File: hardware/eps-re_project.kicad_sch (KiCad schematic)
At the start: 20 parts, among them J1 2053380004, J13 53398-0671, J14 53398-0471, J2 2053380004, J21 205338-0002, J22 205338-0002, J25 205338-0002, J26 205338-0002, J27 205338-0002, J28 205338-0002, J29 205338-0002, J3 53398-0671, J4 2053380004, J5 53398-0471, J6 53398-0471, J7 53398-0471

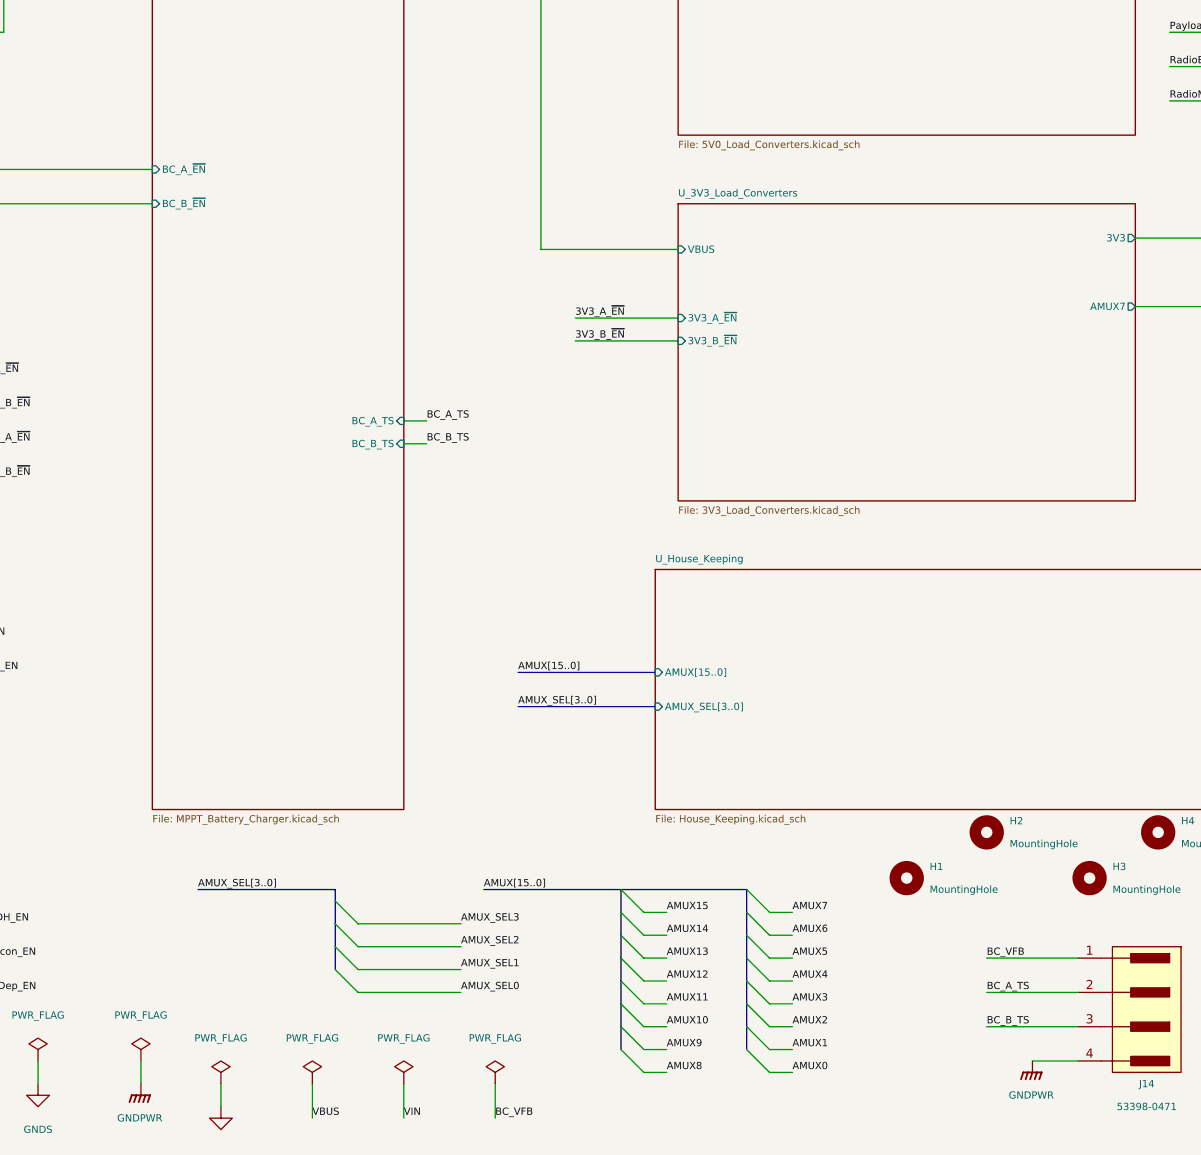
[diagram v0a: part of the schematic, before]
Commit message: hardware: Updating the position of some connectors and components.
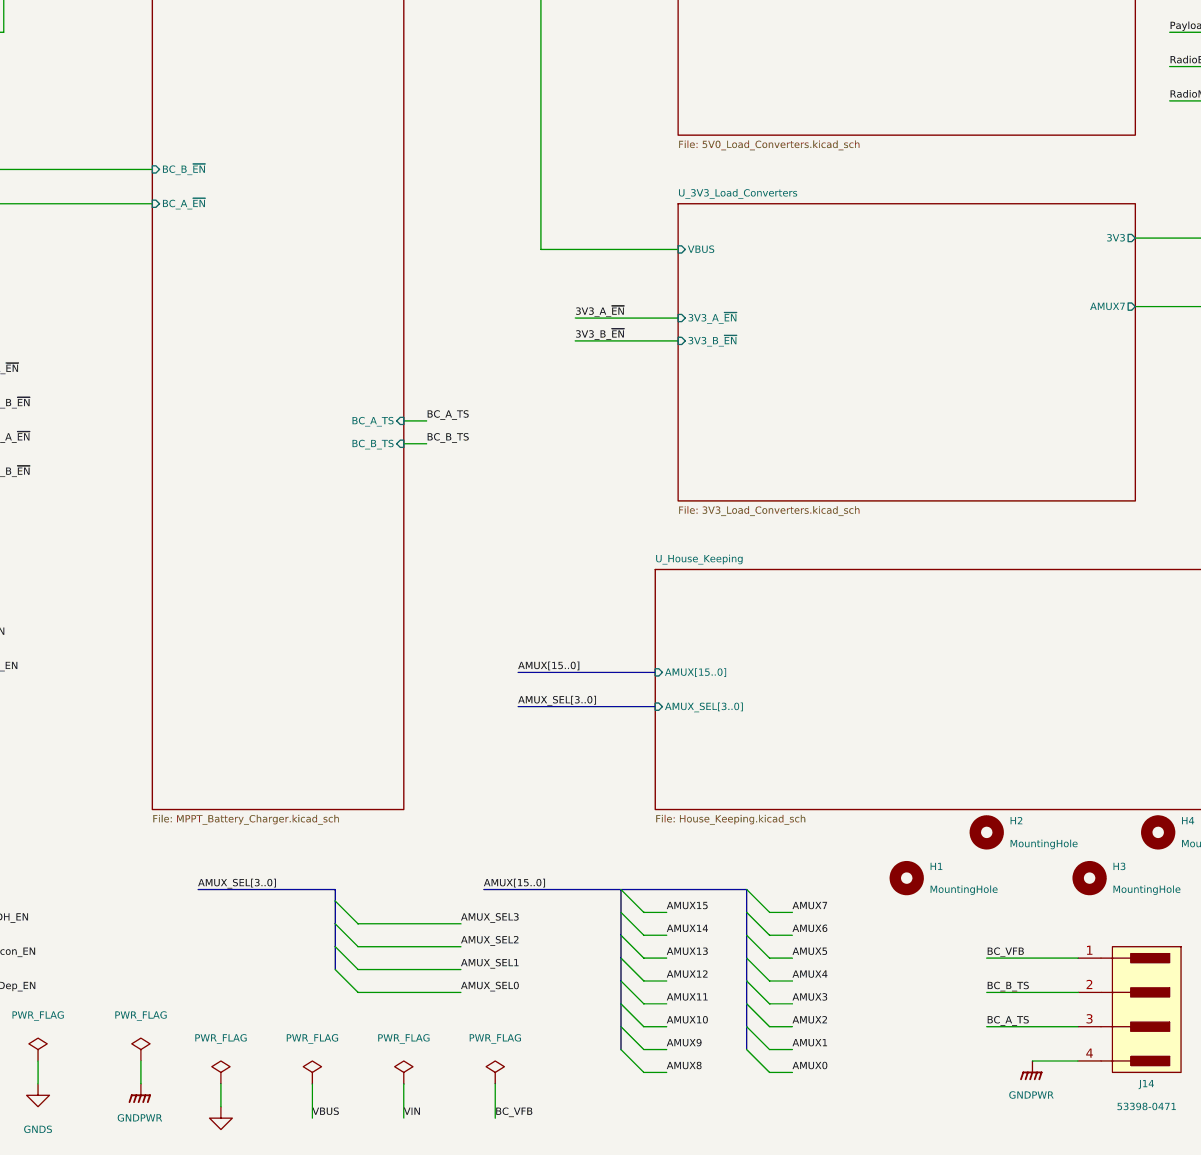
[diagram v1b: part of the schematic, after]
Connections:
- net BC_A_TS: now also J14.3; no longer J14.2
- net BC_B_TS: now also J14.2; no longer J14.3
- net U_MPPT_Batery_Charger/BC_A_~{EN}: now also J5.2; no longer J5.1
- net U_MPPT_Batery_Charger/BC_B_~{EN}: now also J5.1; no longer J5.2
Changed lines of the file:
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@@
     (stroke (width 0) (type default))
   )
-  (wire (pts (xy 29.21 90.17) (xy 57.15 90.17))
-    (stroke (width 0) (type default))
-  )
   (wire (pts (xy 250.19 63.5) (xy 250.19 74.93))
     (stroke (width 0.5) (type default))
@@
     (stroke (width 1) (type default))
   )
-  (wire (pts (xy 29.21 93.98) (xy 57.15 93.98))
+  (wire (pts (xy 29.21 90.17) (xy 57.15 90.17))
     (stroke (width 0) (type default))
   )
@@
     (stroke (width 0.5) (type default))
   )
+  (wire (pts (xy 29.21 93.98) (xy 57.15 93.98))
+    (stroke (width 0) (type default))
+  )
   (wire (pts (xy 170.18 82.55) (xy 186.69 82.55))
     (stroke (width 0) (type default))
@@
     (effects (font (size 0.8 0.8)) (justify left bottom))
   )
-  (label "BC_B_TS" (at 149.86 185.42 0) (fields_autoplaced)
+  (label "BC_A_TS" (at 149.86 185.42 0) (fields_autoplaced)
     (effects (font (size 0.8 0.8)) (justify left bottom))
   )
@@
     (effects (font (size 0.8 0.8)) (justify left bottom))
   )
-  (label "BC_A_TS" (at 149.86 181.61 0) (fields_autoplaced)
+  (label "BC_B_TS" (at 149.86 181.61 0) (fields_autoplaced)
     (effects (font (size 0.8 0.8)) (justify left bottom))
   )
@@
       (effects (font (size 0.8 0.8)) (justify left))
     )
-    (pin "BC_A_~{EN}" input (at 57.15 90.17 180)
+    (pin "BC_A_~{EN}" input (at 57.15 93.98 180)
       (effects (font (size 0.8 0.8)) (justify left))
     )
-    (pin "BC_B_~{EN}" input (at 57.15 93.98 180)
+    (pin "BC_B_~{EN}" input (at 57.15 90.17 180)
       (effects (font (size 0.8 0.8)) (justify left))
     )

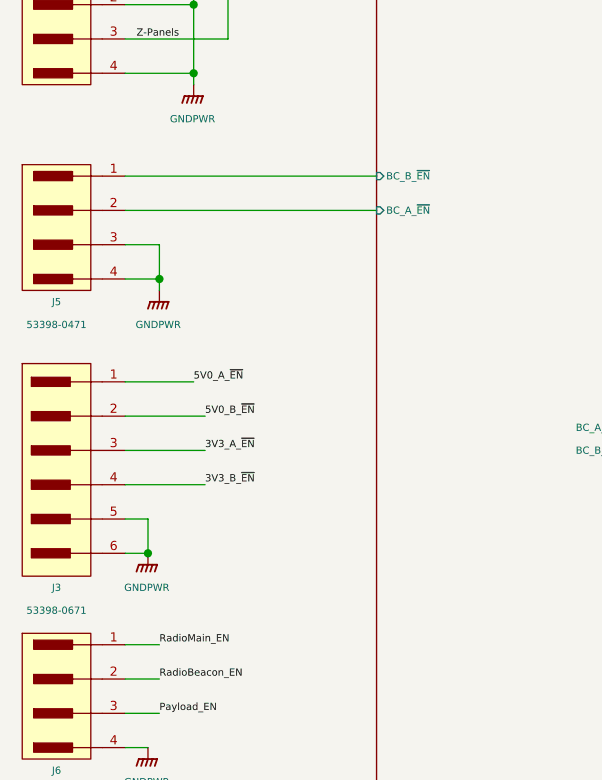
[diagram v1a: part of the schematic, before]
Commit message: hardware: Updating the connectors and connections of the analog signals.
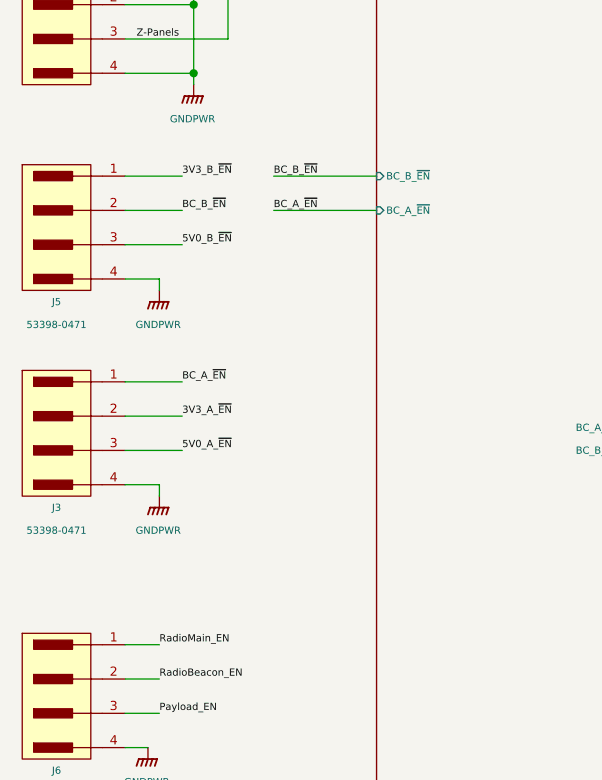
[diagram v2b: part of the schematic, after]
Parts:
- removed J3: 53398-0671, footprints:533980671, symbol 533980671:53398-0671
- added J3: 53398-0471, footprints:533980471, symbol 533980471:533980471_1
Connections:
- net U_MPPT_Batery_Charger/BC_B_~{EN} is gone; now on net 3V3_B_~{EN}: J5.1
- net 3V3_A_~{EN}: now also J3.2
- net 5V0_A_~{EN}: now also J3.3
- net 5V0_B_~{EN}: now also J5.3
- net GNDPWR: now also J3.4; no longer J5.3
- net U_MPPT_Batery_Charger/BC_A_~{EN} renamed BC_B_~{EN}
- new net BC_A_~{EN}: J3.1

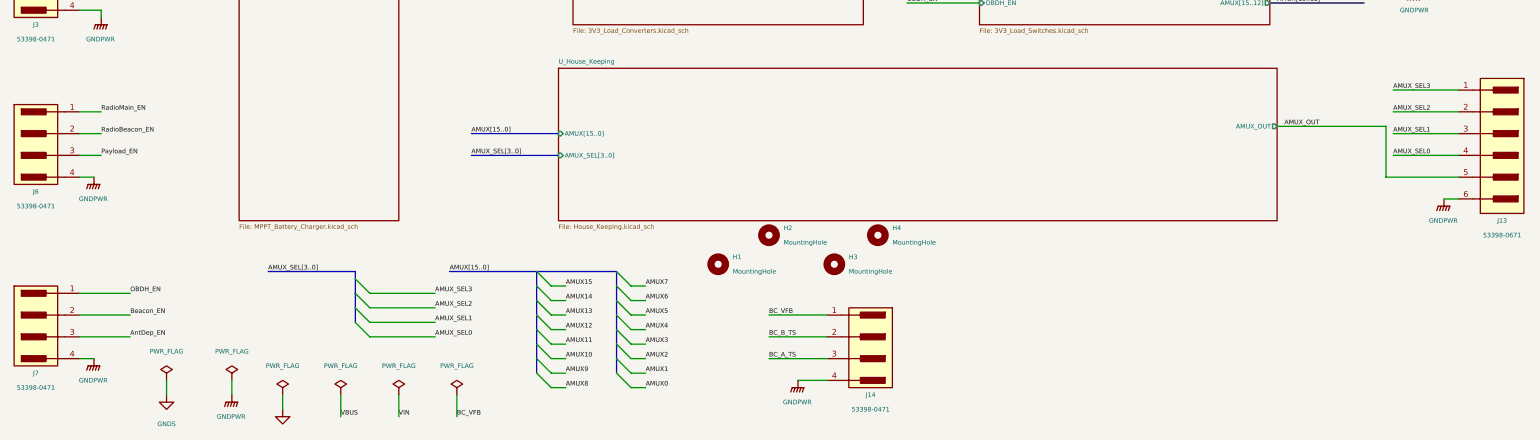
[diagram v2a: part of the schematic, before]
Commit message: hardware: First version of the RE2PS layout with all components connected.
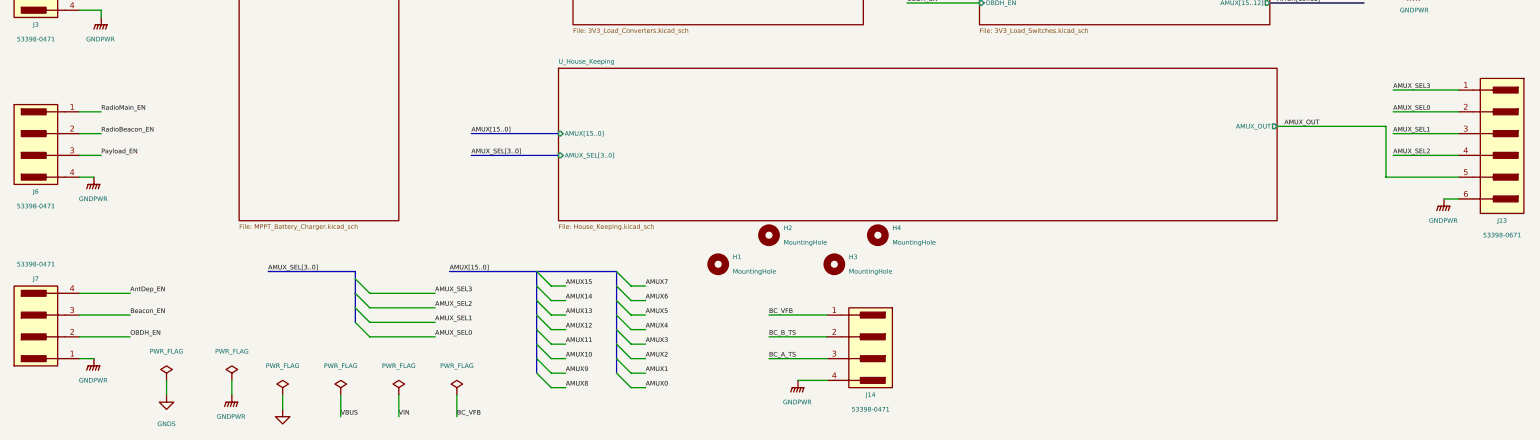
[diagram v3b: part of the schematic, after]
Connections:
- net AMUX_SEL0: now also J13.2; no longer J13.4
- net AMUX_SEL2: now also J13.4; no longer J13.2
- net AntDep_EN: now also J7.4; no longer J7.3
- net Beacon_EN: now also J7.3; no longer J7.2
- net GNDPWR: now also J7.1; no longer J7.4
- net OBDH_EN: now also J7.2; no longer J7.1
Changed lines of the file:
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@@
     (effects (font (size 0.8 0.8)) (justify left bottom))
   )
-  (label "AMUX_SEL2" (at 259.08 142.24 0) (fields_autoplaced)
-    (effects (font (size 0.8 0.8)) (justify left bottom))
-  )
-  (label "AMUX_SEL0" (at 259.08 149.86 0) (fields_autoplaced)
+  (label "AMUX_SEL2" (at 259.08 149.86 0) (fields_autoplaced)
+    (effects (font (size 0.8 0.8)) (justify left bottom))
+  )
+  (label "AMUX_SEL0" (at 259.08 142.24 0) (fields_autoplaced)
     (effects (font (size 0.8 0.8)) (justify left bottom))
   )
@@
     (effects (font (size 0.8 0.8)) (justify left bottom))
   )
-  (label "AntDep_EN" (at 38.1 181.61 0) (fields_autoplaced)
+  (label "AntDep_EN" (at 38.1 173.99 0) (fields_autoplaced)
     (effects (font (size 0.8 0.8)) (justify left bottom))
   )
@@
     (effects (font (size 0.8 0.8)) (justify left bottom))
   )
-  (label "OBDH_EN" (at 38.1 173.99 0) (fields_autoplaced)
+  (label "OBDH_EN" (at 38.1 181.61 0) (fields_autoplaced)
     (effects (font (size 0.8 0.8)) (justify left bottom))
   )
@@
     )
   )
-  (symbol (lib_id "533980471:533980471_1") (at 33.02 182.88 0) (unit 1)
+  (symbol (lib_id "533980471:533980471_1") (at 33.02 176.53 0) (mirror x) (unit 1)
     (in_bom yes) (on_board yes) (dnp no)
-    (property "Reference" "J7" (at 21.59 187.96 0)
-      (effects (font (size 0.8 0.8)))
-    )
-    (property "Value" "53398-0471" (at 21.59 190.5 0)
-      (effects (font (size 0.8 0.8)))
-    )
-    (property "Footprint" "footprints:533980471" (at 33.02 170.18 0)
-      (effects (font (size 0.8 0.8)) (justify left) hide)
-    )
-    (property "Datasheet" "https://www.molex.com/pdm_docs/ps/PS-51021-024-001.pdf" (at 33.02 167.64 0)
-      (effects (font (size 0.8 0.8)) (justify left) hide)
-    )
-    (property "ambient temperature range high" "+105°C" (at 33.02 165.1 0)
-      (effects (font (size 0.8 0.8)) (justify left) hide)
-    )
-    (property "ambient temperature range low" "-40°C" (at 33.02 162.56 0)
-      (effects (font (size 0.8 0.8)) (justify left) hide)
-    )
-    (property "automotive" "No" (at 33.02 160.02 0)
-      (effects (font (size 0.8 0.8)) (justify left) hide)
-    )
-    (property "category" "Conn" (at 33.02 157.48 0)
-      (effects (font (size 0.8 0.8)) (justify left) hide)
-    )
-    (property "contact material" "Tin" (at 33.02 154.94 0)
-      (effects (font (size 0.8 0.8)) (justify left) hide)
-    )
-    (property "current rating" "1A" (at 33.02 152.4 0)
-      (effects (font (size 0.8 0.8)) (justify left) hide)
-    )
-    (property "device class L1" "Connectors" (at 33.02 149.86 0)
-      (effects (font (size 0.8 0.8)) (justify left) hide)
-    )
-    (property "device class L2" "Headers and Wire Housings" (at 33.02 147.32 0)
-      (effects (font (size 0.8 0.8)) (justify left) hide)
-    )
-    (property "device class L3" "unset" (at 33.02 144.78 0)
-      (effects (font (size 0.8 0.8)) (justify left) hide)
-    )
-    (property "digikey description" "CONN HEADER SMD 4POS 1.25MM" (at 33.02 142.24 0)
-      (effects (font (size 0.8 0.8)) (justify left) hide)
-    )
-    (property "digikey part number" "WM7608CT-ND" (at 33.02 139.7 0)
-      (effects (font (size 0.8 0.8)) (justify left) hide)
-    )
-    (property "footprint url" "https://www.molex.com/pdm_docs/sd/533980471_sd.pdf" (at 33.02 137.16 0)
-      (effects (font (size 0.8 0.8)) (justify left) hide)
-    )
-    (property "height" "5.1mm" (at 33.02 134.62 0)
-      (effects (font (size 0.8 0.8)) (justify left) hide)
-    )
-    (property "is connector" "yes" (at 33.02 132.08 0)
-      (effects (font (size 0.8 0.8)) (justify left) hide)
-    )
-    (property "is male" "yes" (at 33.02 129.54 0)
-      (effects (font (size 0.8 0.8)) (justify left) hide)
-    )
-    (property "lead free" "Yes" (at 33.02 127 0)
-      (effects (font (size 0.8 0.8)) (justify left) hide)
-    )
-    (property "library id" "4d2e3deedc0cf3e3" (at 33.02 124.46 0)
-      (effects (font (size 0.8 0.8)) (justify left) hide)
-    )
-    (property "manufacturer" "Molex" (at 33.02 121.92 0)
-      (effects (font (size 0.8 0.8)) (justify left) hide)
-    )
-    (property "mouser part number" "538-53398-0471" (at 33.02 119.38 0)
-      (effects (font (size 0.8 0.8)) (justify left) hide)
-    )
-    (property "number of contacts" "4" (at 33.02 116.84 0)
-      (effects (font (size 0.8 0.8)) (justify left) hide)
-    )
-    (property "number of rows" "1" (at 33.02 114.3 0)
-      (effects (font (size 0.8 0.8)) (justify left) hide)
-    )
-    (property "package" "HDR4" (at 33.02 111.76 0)
-      (effects (font (size 0.8 0.8)) (justify left) hide)
-    )
-    (property "pitch" "1.25mm" (at 33.02 109.22 0)
-      (effects (font (size 0.8 0.8)) (justify left) hide)
-    )
-    (property "rohs" "Yes" (at 33.02 106.68 0)
-      (effects (font (size 0.8 0.8)) (justify left) hide)
-    )
-    (property "standoff height" "0.05mm" (at 33.02 104.14 0)
-      (effects (font (size 0.8 0.8)) (justify left) hide)
-    )
-    (property "temperature range high" "+105°C" (at 33.02 101.6 0)
-      (effects (font (size 0.8 0.8)) (justify left) hide)
-    )
-    (property "temperature range low" "-40°C" (at 33.02 99.06 0)
-      (effects (font (size 0.8 0.8)) (justify left) hide)
-    )
-    (property "voltage rating" "125V" (at 33.02 96.52 0)
-      (effects (font (size 0.8 0.8)) (justify left) hide)
-    )
+    (property "Reference" "J7" (at 21.59 171.45 0)
+      (effects (font (size 0.8 0.8)))
+    )
+    (property "Value" "53398-0471" (at 21.59 168.91 0)
+      (effects (font (size 0.8 0.8)))
+    )
+    (property "Footprint" "footprints:533980471" (at 33.02 189.23 0)
+      (effects (font (size 0.8 0.8)) (justify left) hide)
+    )
+    (property "Datasheet" "https://www.molex.com/pdm_docs/ps/PS-51021-024-001.pdf" (at 33.02 191.77 0)
+      (effects (font (size 0.8 0.8)) (justify left) hide)
+    )
+    (property "ambient temperature range high" "+105°C" (at 33.02 194.31 0)
+      (effects (font (size 0.8 0.8)) (justify left) hide)
+    )
+    (property "ambient temperature range low" "-40°C" (at 33.02 196.85 0)
+      (effects (font (size 0.8 0.8)) (justify left) hide)
+    )
+    (property "automotive" "No" (at 33.02 199.39 0)
+      (effects (font (size 0.8 0.8)) (justify left) hide)
+    )
+    (property "category" "Conn" (at 33.02 201.93 0)
+      (effects (font (size 0.8 0.8)) (justify left) hide)
+    )
+    (property "contact material" "Tin" (at 33.02 204.47 0)
+      (effects (font (size 0.8 0.8)) (justify left) hide)
+    )
+    (property "current rating" "1A" (at 33.02 207.01 0)
+      (effects (font (size 0.8 0.8)) (justify left) hide)
+    )
+    (property "device class L1" "Connectors" (at 33.02 209.55 0)
+      (effects (font (size 0.8 0.8)) (justify left) hide)
+    )
+    (property "device class L2" "Headers and Wire Housings" (at 33.02 212.09 0)
+      (effects (font (size 0.8 0.8)) (justify left) hide)
+    )
+    (property "device class L3" "unset" (at 33.02 214.63 0)
+      (effects (font (size 0.8 0.8)) (justify left) hide)
+    )
+    (property "digikey description" "CONN HEADER SMD 4POS 1.25MM" (at 33.02 217.17 0)
+      (effects (font (size 0.8 0.8)) (justify left) hide)
+    )
+    (property "digikey part number" "WM7608CT-ND" (at 33.02 219.71 0)
+      (effects (font (size 0.8 0.8)) (justify left) hide)
+    )
+    (property "footprint url" "https://www.molex.com/pdm_docs/sd/533980471_sd.pdf" (at 33.02 222.25 0)
+      (effects (font (size 0.8 0.8)) (justify left) hide)
+    )
+    (property "height" "5.1mm" (at 33.02 224.79 0)
+      (effects (font (size 0.8 0.8)) (justify left) hide)
+    )
+    (property "is connector" "yes" (at 33.02 227.33 0)
+      (effects (font (size 0.8 0.8)) (justify left) hide)
+    )
+    (property "is male" "yes" (at 33.02 229.87 0)
+      (effects (font (size 0.8 0.8)) (justify left) hide)
+    )
+    (property "lead free" "Yes" (at 33.02 232.41 0)
+      (effects (font (size 0.8 0.8)) (justify left) hide)
+    )
+    (property "library id" "4d2e3deedc0cf3e3" (at 33.02 234.95 0)
+      (effects (font (size 0.8 0.8)) (justify left) hide)
+    )
+    (property "manufacturer" "Molex" (at 33.02 237.49 0)
+      (effects (font (size 0.8 0.8)) (justify left) hide)
+    )
+    (property "mouser part number" "538-53398-0471" (at 33.02 240.03 0)
+      (effects (font (size 0.8 0.8)) (justify left) hide)
+    )
+    (property "number of contacts" "4" (at 33.02 242.57 0)
+      (effects (font (size 0.8 0.8)) (justify left) hide)
+    )
+    (property "number of rows" "1" (at 33.02 245.11 0)
+      (effects (font (size 0.8 0.8)) (justify left) hide)
+    )
+    (property "package" "HDR4" (at 33.02 247.65 0)
+      (effects (font (size 0.8 0.8)) (justify left) hide)
+    )
+    (property "pitch" "1.25mm" (at 33.02 250.19 0)
+      (effects (font (size 0.8 0.8)) (justify left) hide)
+    )
+    (property "rohs" "Yes" (at 33.02 252.73 0)
+      (effects (font (size 0.8 0.8)) (justify left) hide)
+    )
+    (property "standoff height" "0.05mm" (at 33.02 255.27 0)
+      (effects (font (size 0.8 0.8)) (justify left) hide)
+    )
+    (property "temperature range high" "+105°C" (at 33.02 257.81 0)
+      (effects (font (size 0.8 0.8)) (justify left) hide)
+    )
+    (property "temperature range low" "-40°C" (at 33.02 260.35 0)
+      (effects (font (size 0.8 0.8)) (justify left) hide)
+    )
+    (property "voltage rating" "125V" (at 33.02 262.89 0)
+      (effects (font (size 0.8 0.8)) (justify left) hide)
+    )
